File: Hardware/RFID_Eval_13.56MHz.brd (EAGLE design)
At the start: 118.1 x 53.3 mm, 36 parts, among them U1 DNP_SM130, U3 ARDUINO_SHIELDNOLABELS

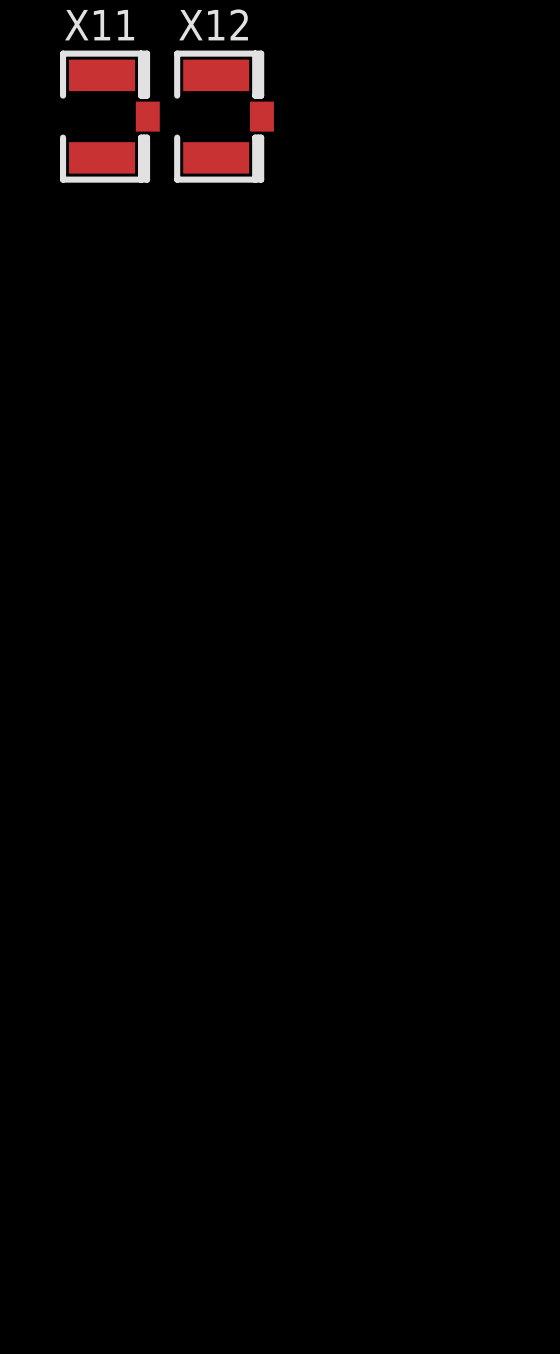
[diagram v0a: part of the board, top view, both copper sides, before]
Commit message: Added 3 more u.FL connectors for testing purpose
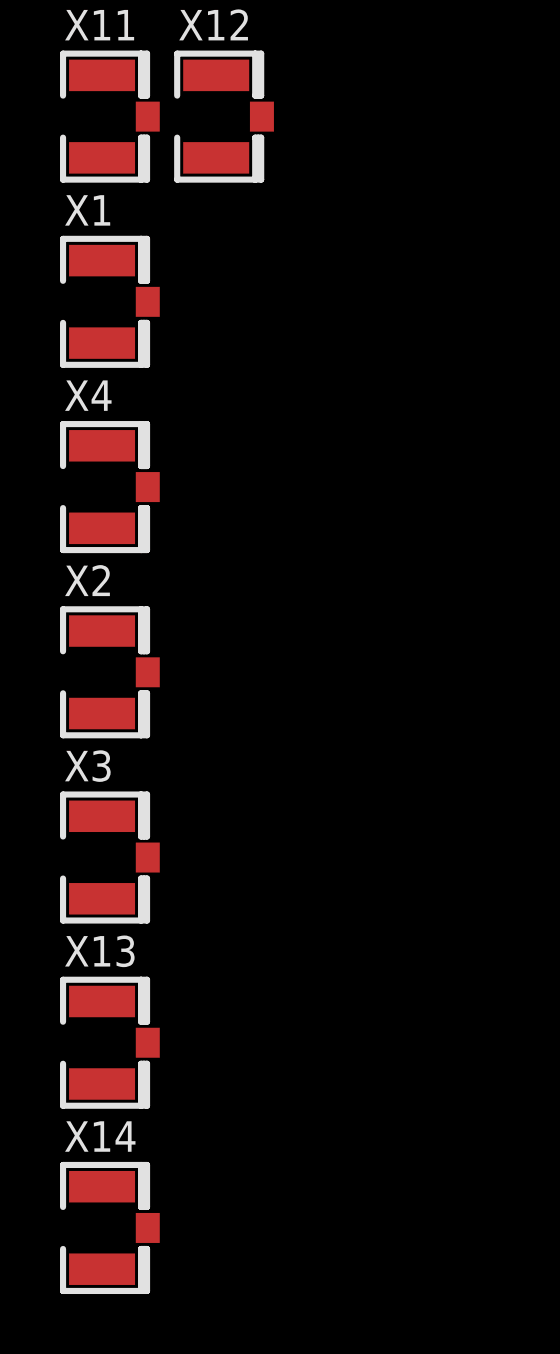
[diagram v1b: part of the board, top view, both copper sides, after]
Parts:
- added X1, X13, X14, X2, X3, X4: (no value), adafruit:U.FL
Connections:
- net ANT1: now also X1.3, X13.3, X2.3
- net ANT2: now also X14.3, X3.3, X4.3
- net GND: now also X1.1, X1.2, X13.1, X13.2, X14.1, X14.2, X2.1, X2.2, X3.1, X3.2, X4.1, X4.2
